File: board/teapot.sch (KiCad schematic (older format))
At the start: 35 parts

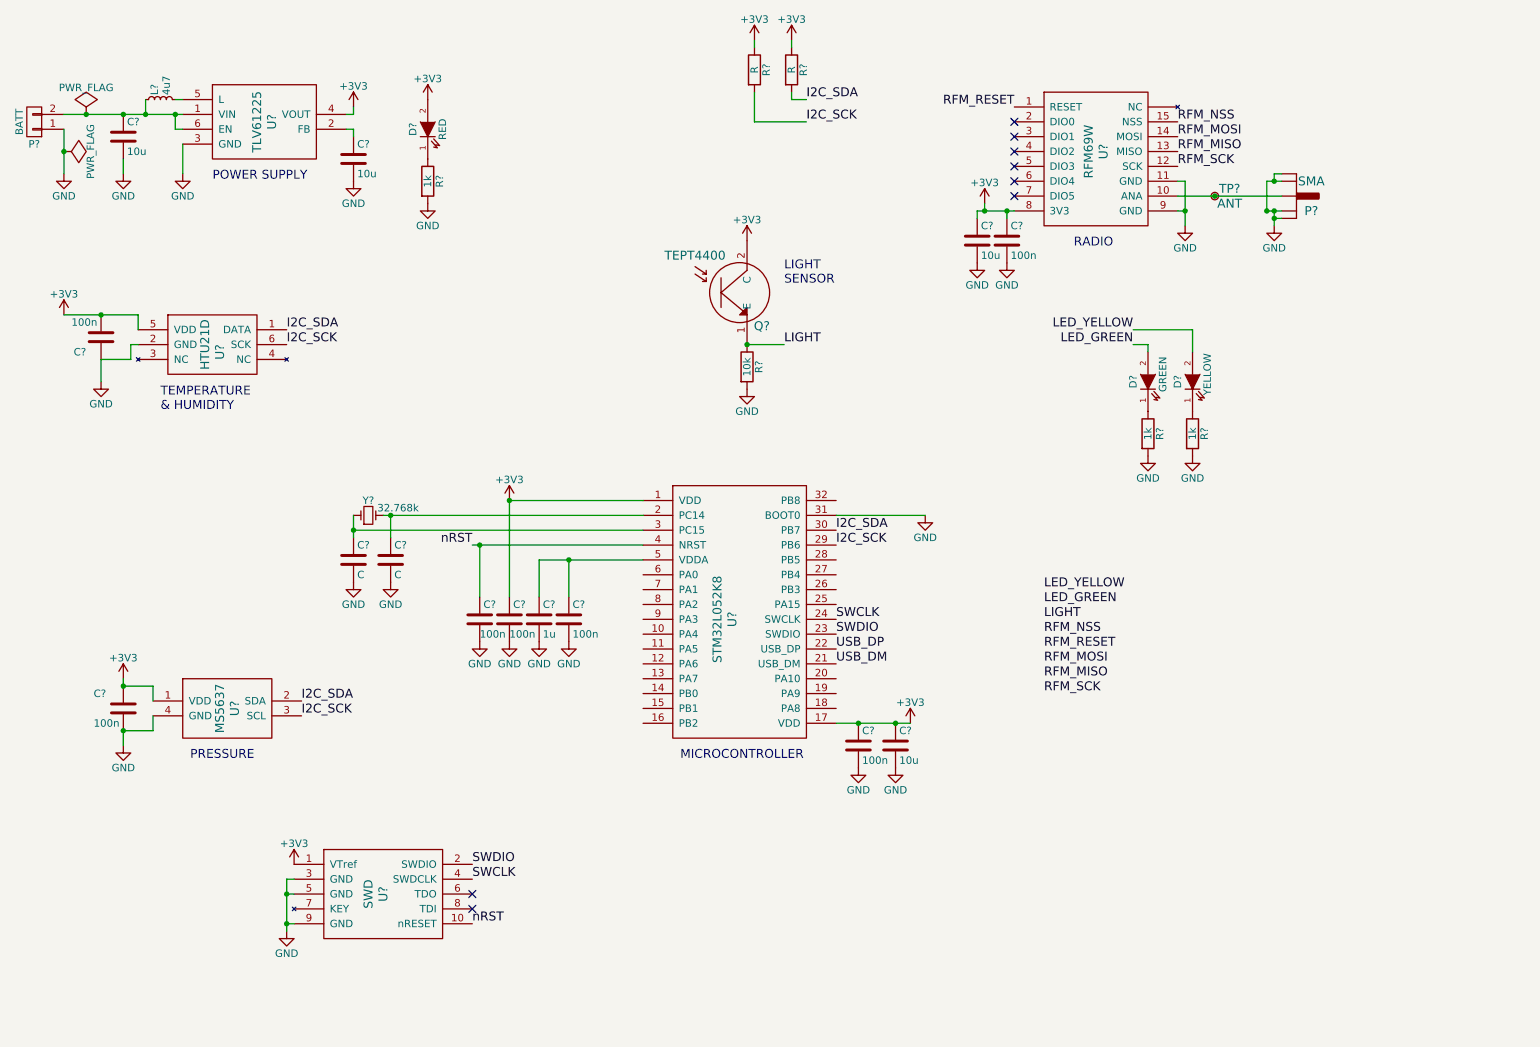
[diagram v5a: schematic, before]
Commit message: Added microusb-b connection
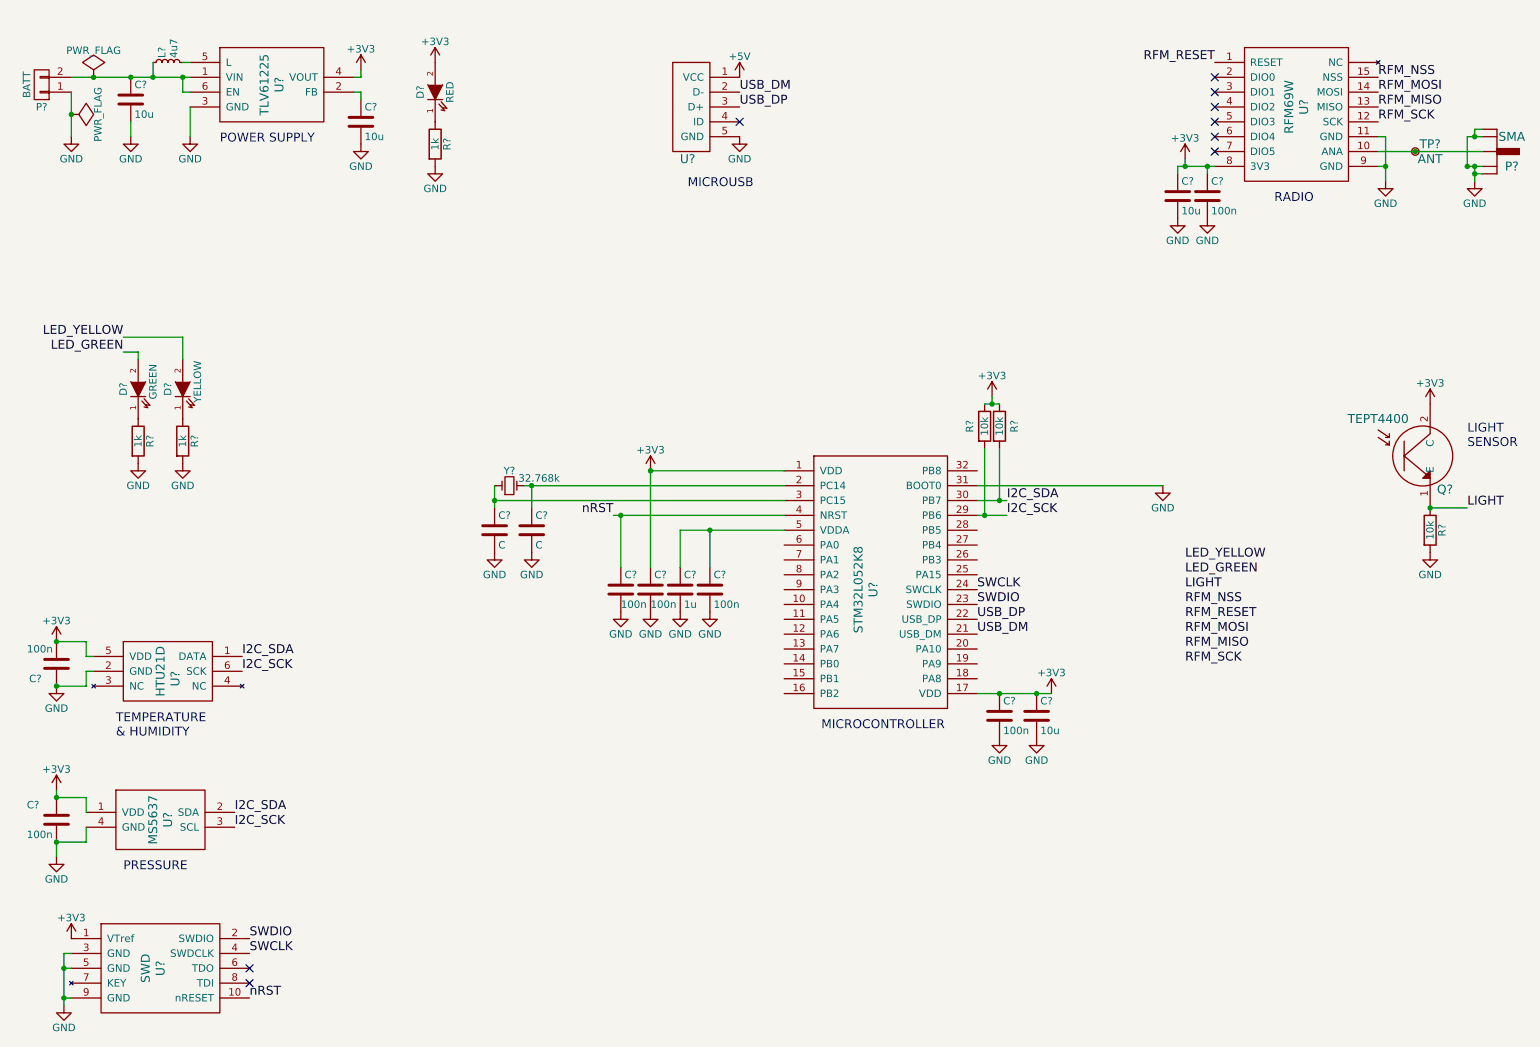
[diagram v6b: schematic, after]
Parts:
- added U?: microusb-b, symbol microusb-b
- R? (x2): value R -> 10k
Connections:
- net GND: now also U?.5 (GND)
- net USB_DM: now also U?.2 (D-)
- net USB_DP: now also U?.3 (D+)
- new net +5V: U?.1 (VCC)
- no-connect marks 8 -> 9
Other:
- note added: "MICROUSB"
- moved on the sheet: C?, D?, L?, P?, Q?, R?, TP?, U?, Y?

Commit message: footprinting
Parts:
- U1: renamed from U?; footprint (none) -> footprints:SC-70
- U3: renamed from U?; footprint (none) -> footprints:RFM69
- U4: renamed from U?; footprint (none) -> footprints:UFQFPN32
- U5: renamed from U?; footprint (none) -> footprints:HTU21D
- U6: renamed from U?; footprint (none) -> footprints:MS563702; Farnell (none) -> 2362663
- U7: renamed from U?; footprint (none) -> footprints:SWD
- gave numbers to parts that had none: 30

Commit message: Footprints and first test board layouts.
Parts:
- P1: footprint (none) -> footprints:AA_holder; Farnell (none) -> 1702629
- P2: footprint (none) -> footprints:SMA-142-0701-801; Farnell (none) -> 1342651
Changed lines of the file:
@@
 F 0 "P1" H 850 1300 50  0000 C CNN
 F 1 "BATT" V 950 1150 50  0000 C CNN
-F 2 "" H 850 1150 50  0000 C CNN
-F 3 "" H 850 1150 50  0000 C CNN
+F 2 "footprints:AA_holder" H 850 1150 50  0001 C CNN
+F 3 "http://www.farnell.com/datasheets/1703957.pdf" H 850 1150 50  0001 C CNN
+F 4 "1702629" H 850 1150 60  0001 C CNN "Farnell"
 	1    850  1150
 	-1   0    0    1
@@
 F 0 "P2" H 10750 1500 60  0000 C CNN
 F 1 "SMA" H 10750 1700 60  0000 C CNN
-F 2 "" H 10650 1600 60  0000 C CNN
+F 2 "footprints:SMA-142-0701-801" H 10650 1600 60  0001 C CNN
 F 3 "" H 10650 1600 60  0000 C CNN
+F 4 "1342651" H 10650 1600 60  0001 C CNN "Farnell"
 	1    10650 1600
 	1    0    0    -1
